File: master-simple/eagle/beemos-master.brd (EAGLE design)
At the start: 99.1 x 73.7 mm, 62 parts, among them CON1 BAT, CON2 JACK_DC_BARREL, CON3 SPI, IC1 32U4, IC2 MCP73831T, IC3 MCP1703CB, IC4 DMP1045U, IC5 MS5637WIDE, J1 RJ123.3, J10 RJ12STRAIGHT-I2C, J2 RJ123.3, J3 RJ123.3, J4 RJ123.3, J5 RJ123.3, J6 RJ123.3, J8 RJ123.3, J9 RJ12STRAIGHT-I2C, X1 8MHz, X2 MINI-USB, X3 1503_09

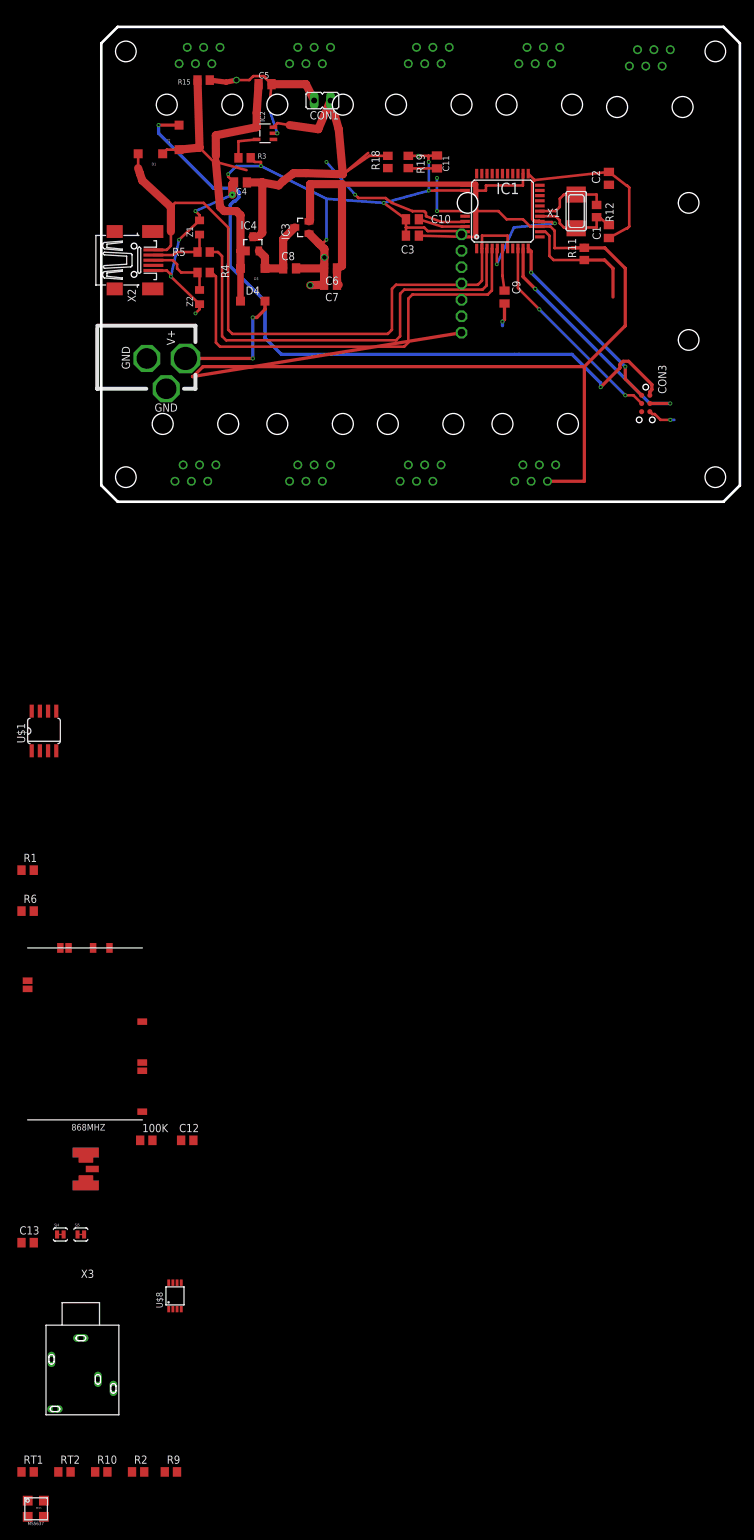
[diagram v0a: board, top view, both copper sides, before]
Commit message: Reorganized components, placement. Cleanup of temporary files
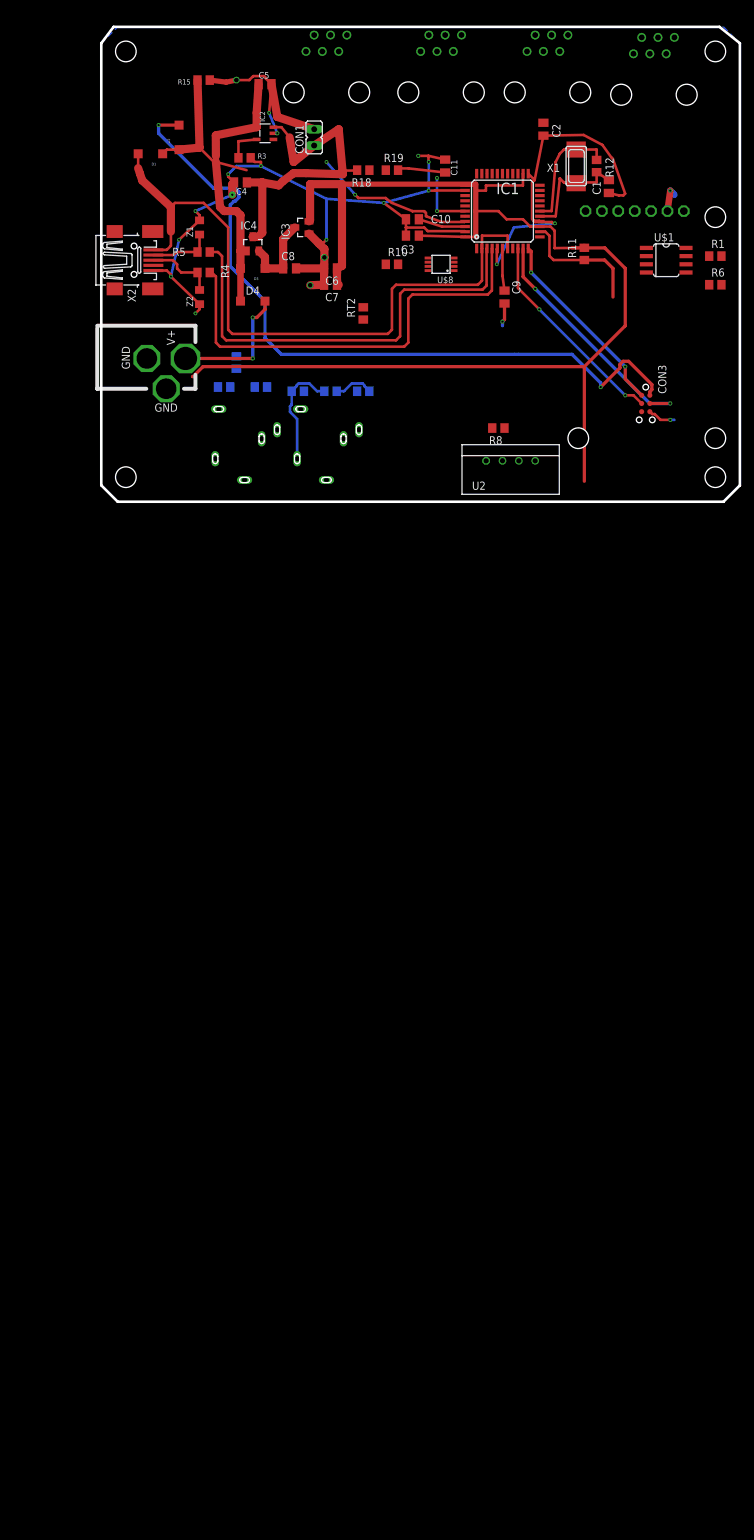
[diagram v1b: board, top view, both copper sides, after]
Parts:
- removed 100K: 100k, rcl:R0805
- removed 868MHZ: (no value), sma_end_launch:SMA_EDGELAUNCH_UFL
- removed C12, C13: 100n, rcl:C0805
- removed IC5: MS5637WIDE, MS5637:MS5637WIDE
- removed J10, J9: RJ12STRAIGHT-I2C, lpatiny:RJ12-STRAIGHT-I2C
- removed J5, J6, J8: RJ123.3, lpatiny:RJ12-STRAIGHT-3.3
- removed SJ4, SJ5: (no value), SparkFun-Passives:PAD-JUMPER-2-NC_BY_TRACE_YES_SILK
- removed U$7: RN2483_SIMPLE, Octanis1_bioreactorPort:RN2483_SIMPLE
- added R13: 100, rcl:R0805
- added R7: 1K, rcl:R0805
- added R8, RT3: 4.7k, resistor:R0805
- added U2: (no value), RHT03_DHT-22_AM2302:RHT03_DHT-22
- added X4: 1503_09, con-lumberg:1503_09
- moved R10 192.7 mm to (45.1, 36.8)
- moved RT2 185.6 mm to (40.6, 29.2), turned to 90 degrees
- moved RT1 174.1 mm to (35.6, 17.1), flipped to the bottom
- moved R2 171.2 mm to (40.6, 17.1), flipped to the bottom
- moved R9 168.8 mm to (30.5, 17.1), flipped to the bottom
- moved U$8 165.3 mm to (52.7, 36.8), turned to 90 degrees
- moved R6 144.3 mm to (95.2, 33.7)
- moved R1 143.0 mm to (95.2, 38.1)
- moved X3 134.4 mm to (34.9, 1.27), flipped to the bottom, turned to 180 degrees
- moved U$1 118.4 mm to (87.6, 35.6), turned to 270 degrees
- moved U$6 27.5 mm to (71.1, 6.99), turned to 90 degrees
- moved C2 12.7 mm to (68.6, 57.8), turned to 90 degrees
- moved C1 6.99 mm to (78.7, 48.9)
- moved R12 6.98 mm to (76.8, 52.1)
- moved X1 6.98 mm to (73.7, 52.1)
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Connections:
- removed net ANGND: 868MHZ.GND@1, 868MHZ.GND@2, 868MHZ.GND@3, 868MHZ.GND@4, C12.2, C13.2, SJ4.2, SJ5.2, U$7.P$1, U$7.P$21, U$7.P$26, U$7.P$27, U$7.P$33
- removed net ANT868: 868MHZ.P, U$7.P$23
- removed net N$27: J8.SCL
- removed net N$28: J8.OUT
- removed net N$29: J8.I/O
- removed net N$30: J8.GND
- removed net N$31: J8.+3.3V
- removed net N$32: J8.SDA
- removed net N$33: J9.+12V
- removed net N$36: J9.GND2
- removed net N$37: J9.+5V
- removed net N$40: J9.GND1
- removed net N$44: J10.+12V
- removed net N$47: J10.GND2
- removed net N$48: J10.+5V
- removed net N$49: J10.GND1
- new net A8: R7.1
- new net N$2: R7.2, RT3.2, X4.2
- new net N$4: R13.1, RT3.1, X4.1
- net 3.3V: now also R13.2; no longer 100K.1, C12.1, C13.1, J5.+3.3V, J6.+3.3V, U$7.P$12
- net A2: no longer 100K.2, U$7.P$32
- net A4: no longer J5.I/O
- net D11: no longer J5.OUT
- net D12: no longer J6.I/O
- net D6: now also R8.1, U2.DATA; no longer J2.OUT
- net D7: now also R8.2, U2.VDD
- net D8: now also J2.OUT; no longer J6.OUT
- net GND: now also U2.GND, X4.3; no longer J5.GND, J6.GND, SJ4.1, SJ5.1
- net RX: no longer U$7.P$6
- net SCL: no longer J10.SCL, J5.SCL, J6.SCL, J9.SCL
- net SDA: no longer J10.SDA, J5.SDA, J6.SDA, J9.SDA
- net TX: no longer U$7.P$7
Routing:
- net 3.3V: track 260.2 -> 212.2 mm
- net N$21: track 0.00 -> 17.2 mm
- net VBAT1: track 62.0 -> 50.3 mm
- net GND: track 212.2 -> 221.5 mm, vias 21 -> 22
- net N$42: track 12.2 -> 18.5 mm
- net N$14: track 0.00 -> 6.16 mm
- net XTAL1: track 13.8 -> 18.3 mm
- net A6: track 4.47 -> 7.45 mm
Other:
- outline, holes or cut-outs redrawn
- board text removed: "Anemometer"
- board text removed: "D11"
- board text removed: "HX711"
- board text removed: "Rain"

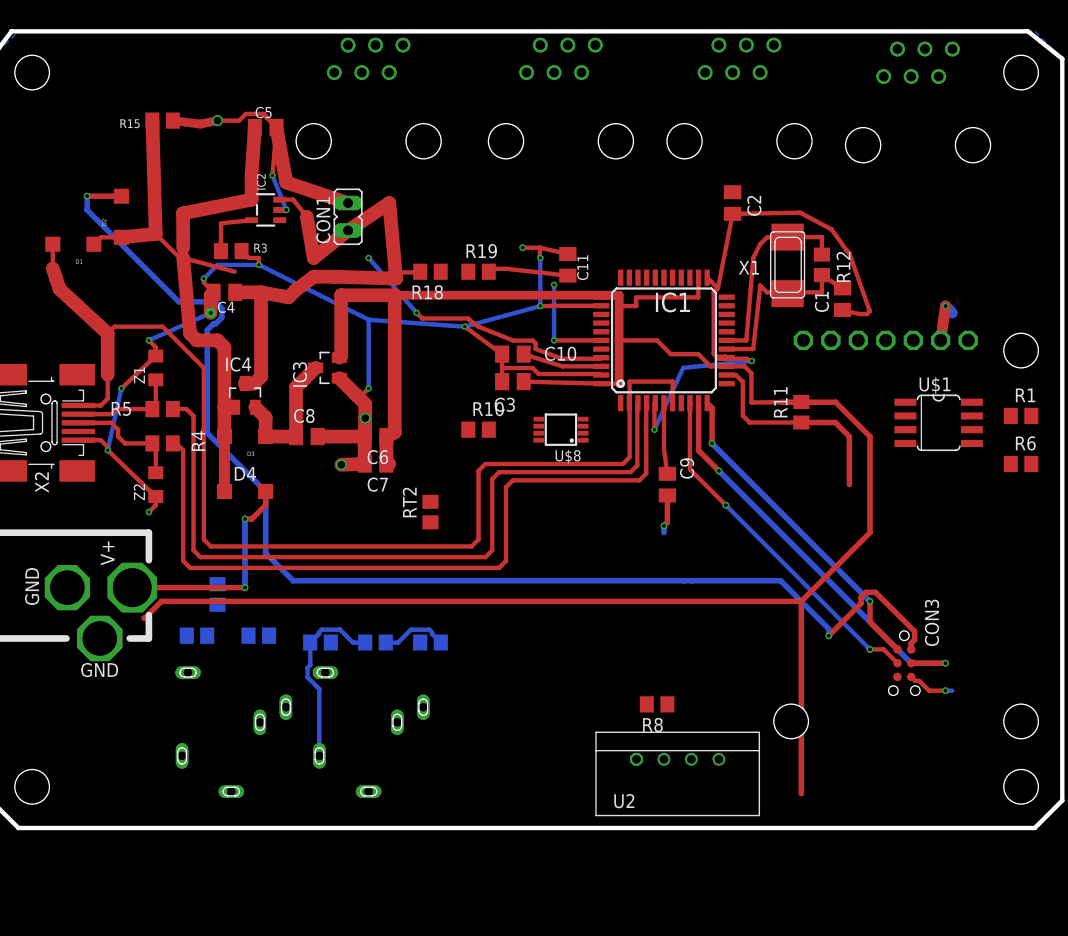
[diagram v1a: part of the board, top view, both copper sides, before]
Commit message: Changed side of RJ12 connectors
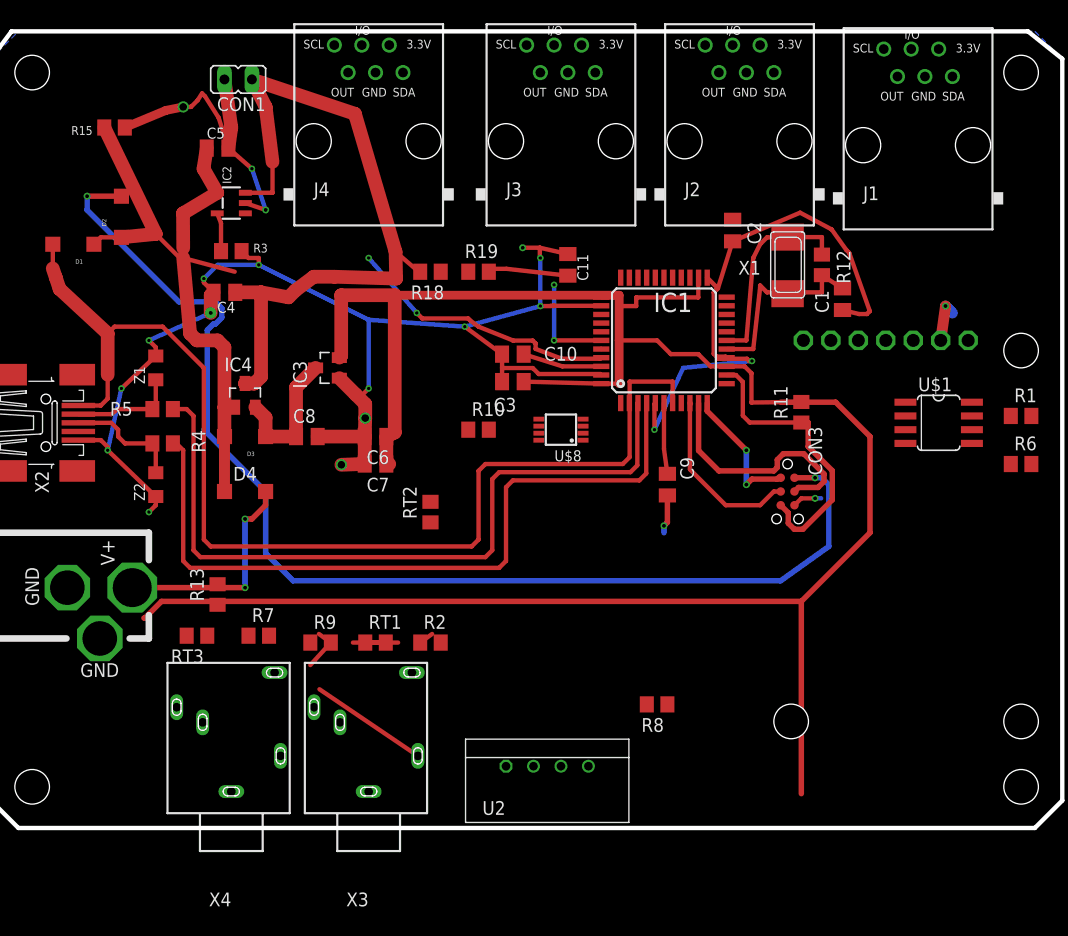
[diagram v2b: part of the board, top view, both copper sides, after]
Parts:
- moved CON3 19.2 mm to (73.7, 33.7)
- moved CON1 16.3 mm to (22.9, 69.2), turned to 90 degrees
- moved U2 12.1 mm to (51.4, 5.71)
- moved C5 4.84 mm to (21.0, 62.9)
- moved R15 4.49 mm to (11.4, 64.8)
- moved IC2 3.24 mm to (22.2, 57.8)
- moved C2 2.54 mm to (68.6, 55.2)
- flipped J1 to the top
- flipped J2 to the top
- flipped J3 to the top
- flipped J4 to the top
- flipped R13 to the top
- flipped R2 to the top
- flipped R7 to the top
- flipped R9 to the top
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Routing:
- net MISO: track 30.1 -> 12.5 mm
- net VBAT1: track 50.3 -> 67.3 mm
- net SCK: track 32.8 -> 16.5 mm, vias 2 -> 0
- net MOSI: track 38.5 -> 22.4 mm, vias 2 -> 0
- net RESET: track 20.0 -> 26.6 mm
- net ISP+5V: track 115.5 -> 110.0 mm
- net GND: track 221.5 -> 216.9 mm
- net N$15: track 66.2 -> 61.7 mm
- net N$6: track 5.41 -> 3.56 mm
- net N$14: track 6.16 -> 4.40 mm
- net N$21: track 17.2 -> 18.2 mm

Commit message: Almost finished beemos master board (labels to do still)
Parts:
- removed U$6: SIM800L, SIM800L:SIP
- removed U$8: DS18B20, lpatiny:MSOP8
- removed U2: (no value), RHT03_DHT-22_AM2302:RHT03_DHT-22
- added JP1: (no value), SparkFun:MOLEX-1X6-RA
- added R14, R16: 10k, rcl:R0805
- added X5: 1503_09, con-lumberg:1503_09
- J1, J2, J3, J4: value RJ123.3 -> RJ12STRAIGHT-I2C; device lpatiny:RJ12-STRAIGHT-3.3 -> lpatiny:RJ12-STRAIGHT-I2C
- R10: value 1K -> 100
- R8: value 4.7k -> 1K; device resistor:R0805 -> rcl:R0805
- moved R7 40.5 mm to (64.8, 24.1), turned to 180 degrees
- moved R10 32.1 mm to (58.4, 7.62)
- moved R6 29.3 mm to (97.2, 62.9), turned to 90 degrees
- moved RT2 28.8 mm to (62.2, 10.2)
- moved R1 24.8 mm to (94.0, 62.9), turned to 90 degrees
- moved C2 11.3 mm to (79.4, 52.1)
- moved U$1 10.5 mm to (85.1, 45.7), turned to 90 degrees
- moved C1 10.0 mm to (88.3, 52.1), turned to 270 degrees
- moved R12 8.89 mm to (85.7, 52.1)
- moved X1 8.89 mm to (82.5, 52.1)
- moved D2 6.75 mm to (6.99, 61.0), turned to 180 degrees
- moved RT3 6.38 mm to (25.4, 17.1), turned to 0 degrees
- moved D1 5.85 mm to (11.4, 49.5)
- moved J1 4.85 mm to (85.1, 67.9), turned to 180 degrees
- moved R13 4.62 mm to (19.7, 17.1), turned to 180 degrees
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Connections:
- removed net A7: R9.1
- removed net A8: R7.1
- removed net D12*: R10.1
- removed net D14: R1.2, R6.2, U$1.8
- removed net N$15: C5.1, D1.C, D2.C, D3.A, D4.C, IC2.4, IC4.1, R15.2
- new net N$5: C5.1, D1.C, D2.C, D3.A, D4.C, IC2.4, IC4.1, R14.1, R15.2
- new net N$7: R16.2
- new net N$8: R8.2, RT2.2, X5.2
- net 3.3V: now also R10.2; no longer J1.+3.3V, J2.+3.3V, J3.+3.3V, J4.+3.3V, RT2.1, U$6.7, U$8.8
- net A0: no longer J1.I/O
- net A1: no longer J2.I/O
- net A2: no longer J3.I/O
- net A3: no longer J4.I/O
- net A5: now also R14.2, R16.1
- net D10: now also R9.1; no longer J4.OUT
- net D11: now also R7.1
- net D5: no longer J1.OUT
- net D6: now also JP1.3; no longer R8.1, U2.DATA
- net D7: now also R8.1; no longer R8.2, U2.VDD
- net D8: no longer J2.OUT
- net D9: now also U$1.8; no longer J3.OUT
- net GND: now also J1.GND1, J1.GND2, J2.GND1, J2.GND2, J3.GND1, J3.GND2, J4.GND1, J4.GND2, JP1.6, X5.3; no longer J1.GND, J2.GND, J3.GND, J4.GND, U$6.2, U$6.6, U$8.4, U2.GND
- net N$9: now also R10.1, RT2.1, X5.1; no longer R10.2, RT2.2, U$8.1
- net RX: now also JP1.5; no longer U$6.4
- net TX: now also JP1.4; no longer U$6.5
- net VBAT1: now also JP1.2; no longer U$6.3
- net VDD: now also J1.+5V, J2.+5V, J3.+5V, J4.+5V, R1.2, R6.2
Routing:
- net VDD: track 13.0 -> 150.0 mm, vias 0 -> 3
- net SCL: track 0.00 -> 115.4 mm, vias 0 -> 3
- net GND: track 216.9 -> 119.5 mm, vias 22 -> 25
- net SDA: track 0.00 -> 89.3 mm, vias 0 -> 4
- net N$5: track 0.00 -> 83.0 mm, vias 0 -> 2
- net D6: track 0.00 -> 76.9 mm, vias 0 -> 2
- net N$2: track 0.00 -> 75.1 mm, vias 0 -> 2
- net VBAT1: track 67.3 -> 142.0 mm, vias 0 -> 2
- net D10: track 0.00 -> 62.5 mm, vias 0 -> 4
- net N$15: track 61.7 -> 0.00 mm
- net TX: track 0.00 -> 53.3 mm, vias 0 -> 2
- net RX: track 0.00 -> 47.5 mm, vias 0 -> 2
- net D7: track 0.00 -> 31.0 mm, vias 0 -> 4
- net D9: track 0.00 -> 26.3 mm, vias 0 -> 2
- net D11: track 0.00 -> 23.4 mm, vias 0 -> 2
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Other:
- board text added: "BeeMoS master v1.0"
- board text removed: "5V"
- board text removed: "BeeMoS Master V 1.0"
- board text removed: "BeeMoS Master V1.0"
- board text removed: "DHT22"
- board text removed: "I2C"
- board text removed: "Microphone"
- board text removed: "OneWire"

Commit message: Repositioned labels on the board layout
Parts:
- CON1: value BAT -> BATTERY
- D1, D2, D3: value Schottky -> Schottky||
- D4: value Schottky -> ||Schottky
- X3, X4, X5: value 1503_09 -> (none)
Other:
- board text added: "BeeMoS I2C master v1.0"
- board text added: "D10"
- board text added: "D11"
- board text added: "D7"
- board text added: "SIM800L"
- board text removed: "BeeMoS master v1.0"
